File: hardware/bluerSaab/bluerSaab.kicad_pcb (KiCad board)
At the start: 2 copper layers, 5 parts, among them U1 LM2596, U2 PCM5102, U3 ESP32-DEVKITC, U4 MCP2515

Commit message: some tracing done
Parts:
- added F1: Fuse, Fuse:Fuseholder_Cylinder-5x20mm_Stelvio-Kontek_PTF78_Horizontal_Open, F.Cu at (99.1, 86.4)
- added J1: Conn_01x12, bluerSaab:SAAB_CDC, F.Cu at (88.9, 53.3)
- moved JP1 70.5 mm to (140.2, 68.6)
- moved U4 63.7 mm to (125.7, 43.2)
- moved U1 63.7 mm to (114.3, 69.8)
- moved U2 63.7 mm to (133.3, 73.7)
- moved U3 62.5 mm to (167.6, 62.2)
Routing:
- net /GND: track 0.00 -> 162.1 mm
- net /5V: track 0.00 -> 91.5 mm
- net /AUDIO_RIGHT: track 0.00 -> 49.8 mm
- net /AUDIO_COMM: track 0.00 -> 49.6 mm, vias 0 -> 2
- net /AUDIO_LEFT: track 0.00 -> 38.5 mm
- net /CAN_L: track 0.00 -> 32.4 mm
- net /CAN_H: track 0.00 -> 32.3 mm
- net /CAR_12V: track 0.00 -> 22.1 mm
- net /CAR_GND: track 0.00 -> 17.6 mm
- net Net-(JP1-Pad1): track 0.00 -> 16.9 mm, vias 0 -> 1
- net /CAN_SCK: track 0.00 -> 16.5 mm
- net /CAN_MOSI: track 0.00 -> 16.5 mm
- net /CAN_MISO: track 0.00 -> 16.3 mm
- net /LCK: track 0.00 -> 14.1 mm
- net /BCK: track 0.00 -> 14.1 mm
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
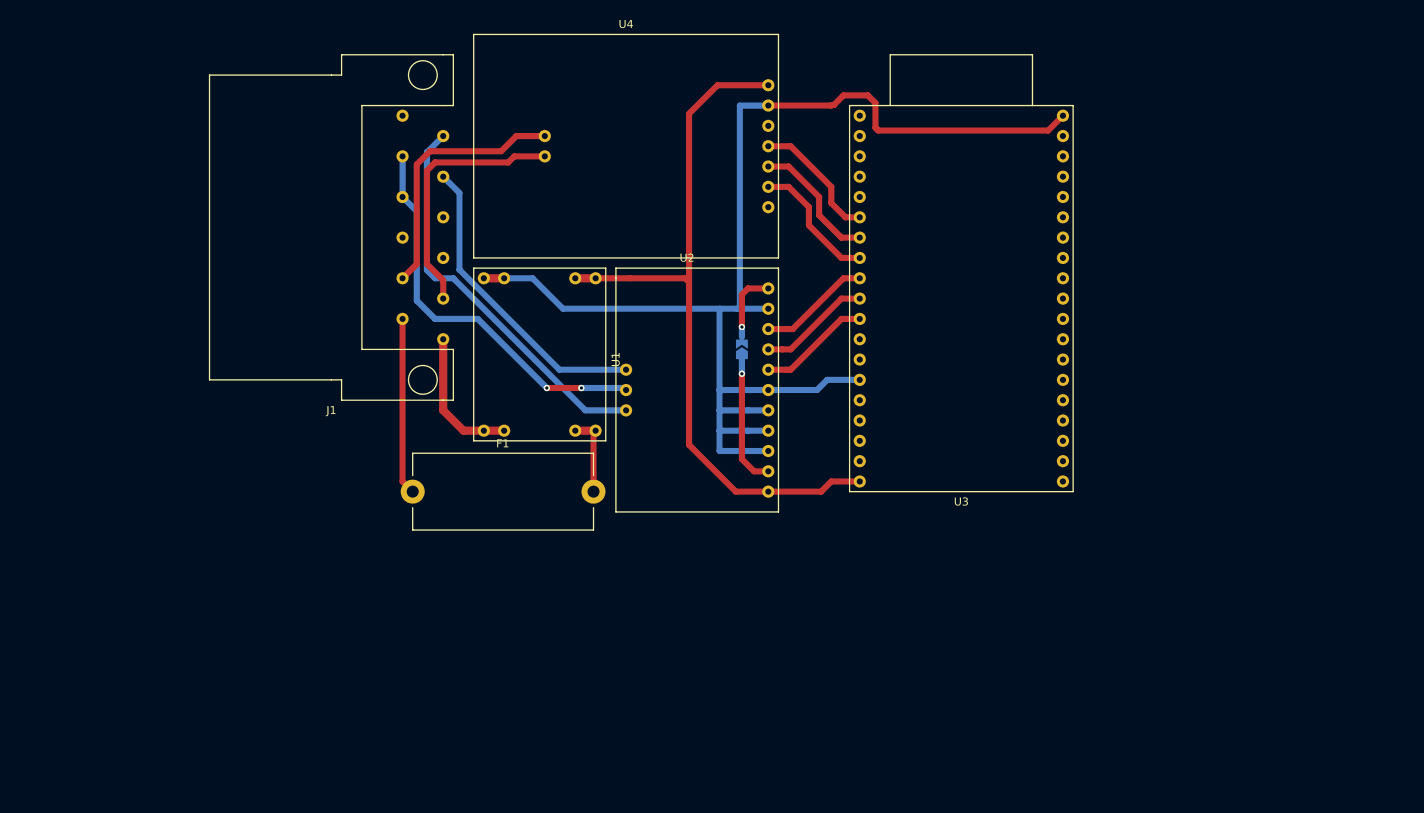
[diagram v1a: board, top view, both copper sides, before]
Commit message: Footprints fixed, PCB done
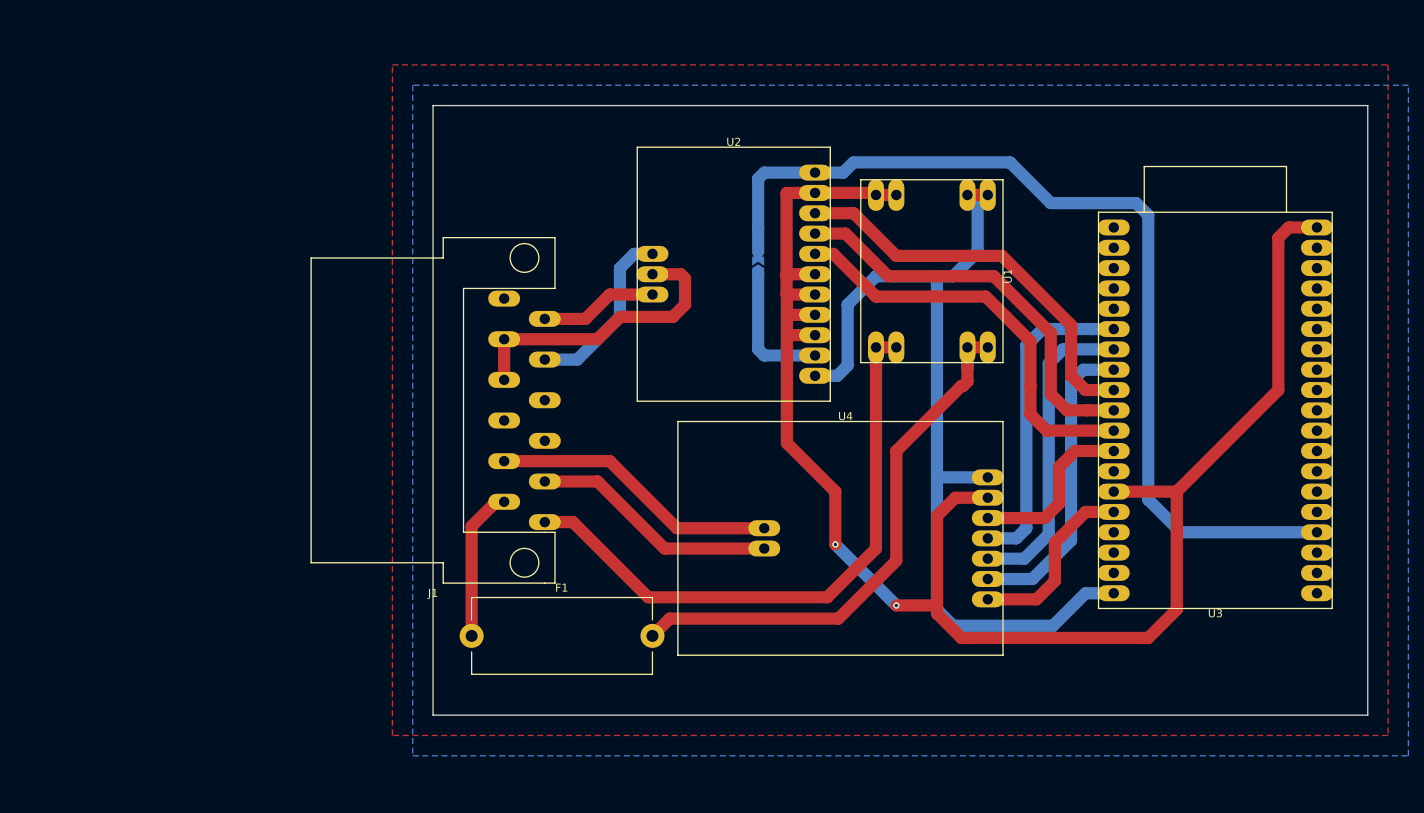
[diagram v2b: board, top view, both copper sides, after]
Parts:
- moved U4 56.2 mm to (153.2, 92.2)
- moved U1 50.1 mm to (163.3, 59.4)
- moved U3 34.7 mm to (199.4, 76.2)
- moved J1 26.2 mm to (101.6, 76.2)
- moved F1 19.5 mm to (106.4, 104.4)
- moved U2 15.6 mm to (139.2, 59.2)
- moved JP1 10.6 mm to (142.2, 58.2)
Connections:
- J1 pad 1: Net-(J1-Pad1) -> (no net)
- J1 pad 10: Net-(J1-Pad10) -> (no net)
- J1 pad 4: Net-(J1-Pad4) -> (no net)
- J1 pad 9: Net-(J1-Pad9) -> (no net)
- U3 pad 1: Net-(U3-Pad1) -> (no net)
- U3 pad 13: Net-(U3-Pad13) -> (no net)
- U3 pad 16: Net-(U3-Pad16) -> (no net)
- U3 pad 17: Net-(U3-Pad17) -> (no net)
- U3 pad 18: Net-(U3-Pad18) -> (no net)
- U3 pad 2: Net-(U3-Pad2) -> (no net)
- U3 pad 20: Net-(U3-Pad20) -> (no net)
- U3 pad 21: Net-(U3-Pad21) -> (no net)
- U3 pad 22: Net-(U3-Pad22) -> (no net)
- U3 pad 24: Net-(U3-Pad24) -> (no net)
- U3 pad 25: Net-(U3-Pad25) -> (no net)
- U3 pad 26: Net-(U3-Pad26) -> (no net)
- U3 pad 27: Net-(U3-Pad27) -> (no net)
- U3 pad 28: Net-(U3-Pad28) -> (no net)
- U3 pad 29: Net-(U3-Pad29) -> (no net)
- U3 pad 3: Net-(U3-Pad3) -> (no net)
- U3 pad 30: Net-(U3-Pad30) -> (no net)
- U3 pad 31: Net-(U3-Pad31) -> (no net)
- U3 pad 32: Net-(U3-Pad32) -> (no net)
- U3 pad 33: Net-(U3-Pad33) -> (no net)
- U3 pad 34: Net-(U3-Pad34) -> (no net)
- U3 pad 35: Net-(U3-Pad35) -> (no net)
- U3 pad 36: Net-(U3-Pad36) -> (no net)
- U3 pad 37: Net-(U3-Pad37) -> (no net)
- U3 pad 4: Net-(U3-Pad4) -> (no net)
- U3 pad 5: Net-(U3-Pad5) -> (no net)
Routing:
- net /XMT: track 9.75 -> 120.9 mm, vias 1 -> 0
- net /CAR_GND: track 17.6 -> 77.5 mm
- net Net-(F1-Pad2): track 10.3 -> 69.2 mm
- net /GND: track 162.1 -> 207.8 mm, vias 0 -> 2
- net /BCK: track 14.1 -> 51.8 mm
- net /DIN: track 14.1 -> 51.0 mm
- net /LCK: track 14.1 -> 50.2 mm
- net /AUDIO_RIGHT: track 49.8 -> 14.7 mm
- net /CAN_MISO: track 16.3 -> 40.0 mm
- net /5V: track 91.5 -> 115.0 mm
- net /CAN_INT: track 0.00 -> 23.1 mm
- net /CAN_MOSI: track 16.5 -> 39.1 mm
- net /CAN_CS: track 0.00 -> 21.9 mm
- net /CAN_SCK: track 16.5 -> 38.2 mm
- net /AUDIO_LEFT: track 38.5 -> 22.5 mm
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- added copper zone on B.Cu, net /GND
- added copper zone on F.Cu, net /GND
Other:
- board outline added: 116.8 x 76.2 mm

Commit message: PCB minified to bring the size below 10x10cm
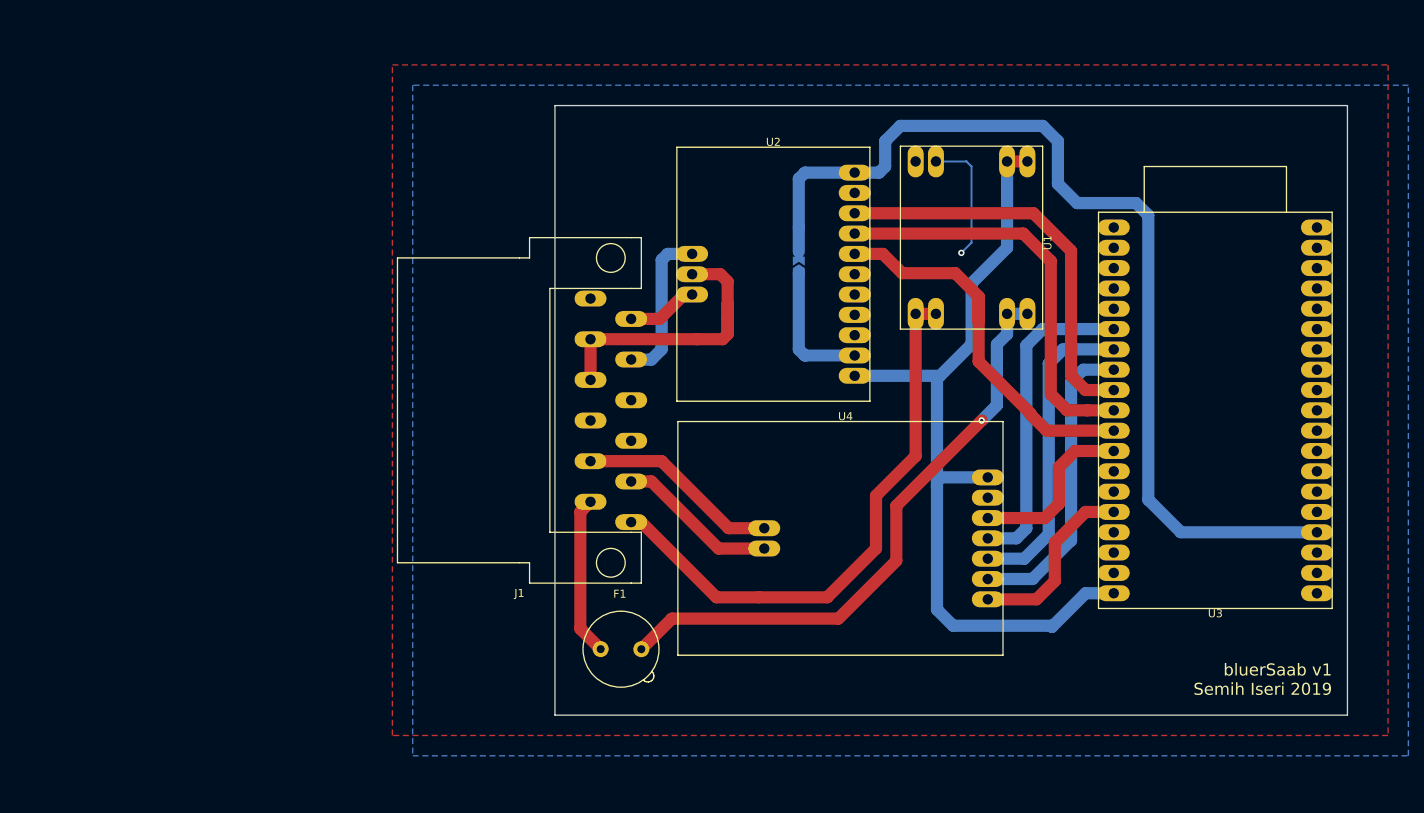
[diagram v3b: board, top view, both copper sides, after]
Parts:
- F1: footprint Fuse:Fuseholder_Cylinder-5x20mm_Stelvio-Kontek_PTF78_Horizontal_Open -> Fuse_Holders_and_Fuses:Fuseholder_Fuse_TR5_Littlefuse-No560_No460
- moved F1 16.2 mm to (122.6, 106.0)
- moved J1 10.8 mm to (112.4, 76.2)
- moved U1 6.49 mm to (168.3, 55.2)
- moved JP1 5.08 mm to (147.3, 58.2)
- moved U2 4.95 mm to (144.1, 59.2)
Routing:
- net /GND: track 207.8 -> 16.0 mm, vias 2 -> 1
- net /CAN_H: track 30.9 -> 20.1 mm
- net /CAN_L: track 36.0 -> 25.2 mm
- net /5V: track 115.0 -> 105.1 mm
- net /CAR_GND: track 77.5 -> 71.0 mm
- net Net-(F1-Pad2): track 69.2 -> 75.6 mm, vias 0 -> 1
- net /AUDIO_RIGHT: track 14.7 -> 8.88 mm
- net /XMT: track 120.9 -> 124.6 mm
- net /AUDIO_LEFT: track 22.5 -> 19.6 mm
- net /BCK: track 51.8 -> 49.5 mm
- net /CAR_12V: track 19.0 -> 20.0 mm
- net /AUDIO_COMM: track 37.0 -> 37.7 mm
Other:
- board size 116.8 x 76.2 mm -> 99.1 x 76.2 mm
- board text added: "bluerSaab v1 Semih Iseri 2019"

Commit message: Via sizes fixed
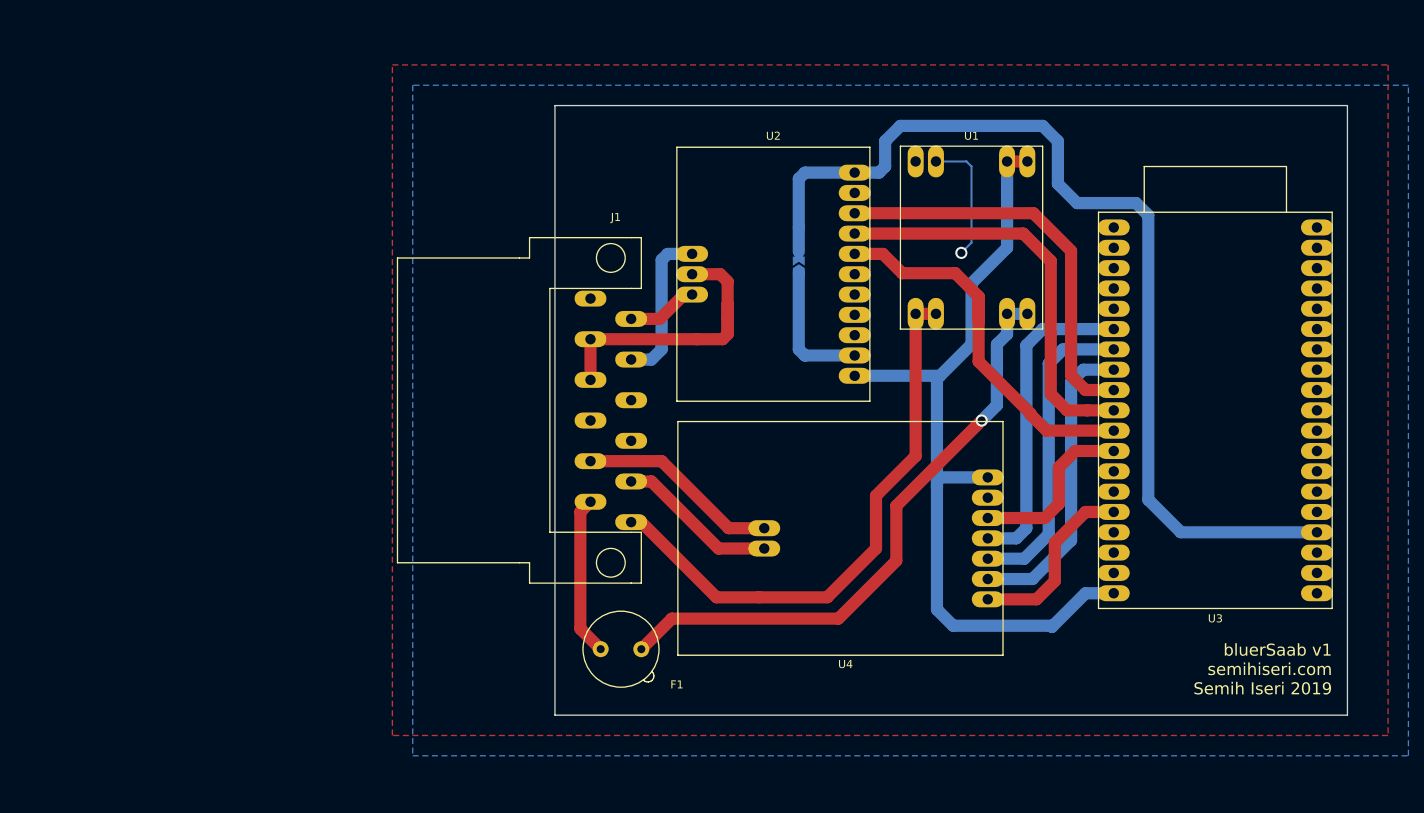
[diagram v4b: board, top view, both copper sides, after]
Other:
- board text added: "bluerSaab v1 semihiseri.com Semih Iseri 2019"
- board text removed: "bluerSaab v1 Semih Iseri 2019"
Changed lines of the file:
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@@
   )
   (setup
-    (last_trace_width 1.524)
+    (last_trace_width 0.25)
     (user_trace_width 0.254)
     (user_trace_width 0.508)
@@
     (visible_elements 7FFFFFFF)
     (pcbplotparams
-      (layerselection 0x010fc_ffffffff)
+      (layerselection 0x010f0_ffffffff)
       (usegerberextensions false)
       (usegerberattributes false)
@@
       (outputformat 1)
       (mirror false)
-      (drillshape 1)
+      (drillshape 0)
       (scaleselection 1)
-      (outputdirectory ""))
+      (outputdirectory "manuf/"))
   )
   (net 0 "")
@@
   (module bluerSaab:PCM5102 locked (layer F.Cu)
     (at 144.145 59.182 180)
-    (fp_text reference U2 (at 0 16.51) (layer F.SilkS)
+    (fp_text reference U2 (at 0 17.272) (layer F.SilkS)
       (effects (font (size 1 1) (thickness 0.15)))
     )
@@
   (module bluerSaab:MCP2515 locked (layer F.Cu)
     (at 153.162 92.202 180)
-    (fp_text reference U4 (at 0 15.24) (layer F.SilkS)
+    (fp_text reference U4 (at 0 -15.748) (layer F.SilkS)
       (effects (font (size 1 1) (thickness 0.15)))
     )
@@
   (module bluerSaab:LM2596 locked (layer F.Cu)
     (at 168.275 55.245 90)
-    (fp_text reference U1 (at 0 10.16 90) (layer F.SilkS)
+    (fp_text reference U1 (at 13.335 0.635 180) (layer F.SilkS)
       (effects (font (size 1 1) (thickness 0.15)))
     )
@@
   (module bluerSaab:ESP32-DEVKITC locked (layer F.Cu)
     (at 199.39 76.2)
-    (fp_text reference U3 (at 0 25.4) (layer F.SilkS)
+    (fp_text reference U3 (at 0 26.035) (layer F.SilkS)
       (effects (font (size 1 1) (thickness 0.15)))
     )
@@
   (module bluerSaab:SAAB_CDC locked (layer F.Cu)
     (at 112.395 76.2)
-    (fp_text reference J1 (at 0 22.86 180) (layer F.SilkS)
+    (fp_text reference J1 (at 12.065 -24.13) (layer F.SilkS)
       (effects (font (size 1 1) (thickness 0.15)))
     )
@@
     (descr "Fuse, Fuseholder, TR5, Littlefuse/Wickmann, No. 460, No560,")
     (tags "Fuse Fuseholder TR5 Littlefuse/Wickmann No. 460 No560 ")
-    (fp_text reference F1 (at 2.39 -6.89) (layer F.SilkS)
+    (fp_text reference F1 (at 9.525 4.445) (layer F.SilkS)
       (effects (font (size 1 1) (thickness 0.15)))
     )
@@
       (net 20 /CAR_12V))
   )
-  (gr_text "bluerSaab v1\nSemih Iseri 2019" (at 213.995 109.855) (layer F.SilkS)
+  (gr_text "bluerSaab v1\nsemihiseri.com\nSemih Iseri 2019" (at 213.995 108.585) (layer F.SilkS)
     (effects (font (size 1.5 1.5) (thickness 0.3)) (justify right))
   )
@@
   (segment (start 168.275 45.085) (end 168.91 45.72) (width 0.254) (layer B.Cu) (net 4))
   (segment (start 168.91 45.72) (end 168.91 55.245) (width 0.254) (layer B.Cu) (net 4))
-  (via (at 167.64 56.515) (size 0.8) (drill 0.4) (layers F.Cu B.Cu) (net 4))
+  (via (at 167.64 56.515) (size 1.524) (drill 1.016) (layers F.Cu B.Cu) (net 4))
   (segment (start 168.91 55.245) (end 167.64 56.515) (width 0.254) (layer B.Cu) (net 4))
   (segment (start 173.355 64.135) (end 175.895 64.135) (width 1.524) (layer B.Cu) (net 5))
-  (via (at 170.18 77.47) (size 0.8) (drill 0.4) (layers F.Cu B.Cu) (net 5))
+  (via (at 170.18 77.47) (size 1.524) (drill 1.016) (layers F.Cu B.Cu) (net 5))
   (segment (start 173.355 66.675) (end 173.355 64.135) (width 1.524) (layer B.Cu) (net 5))
   (segment (start 172.085 67.945) (end 173.355 66.675) (width 1.524) (layer B.Cu) (net 5))
